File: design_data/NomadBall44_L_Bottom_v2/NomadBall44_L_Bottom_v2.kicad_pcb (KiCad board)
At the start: 2 copper layers, 149 x 96.5 mm, 57 parts, among them SW1 SW_Push, SW10 SW_Push, SW11 SW_Push, SW12 SW_Push, SW13 SW_Push, SW14 SW_Push, SW15 SW_Push, SW16 SW_Push, SW17 SW_Push, SW18 SW_Push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

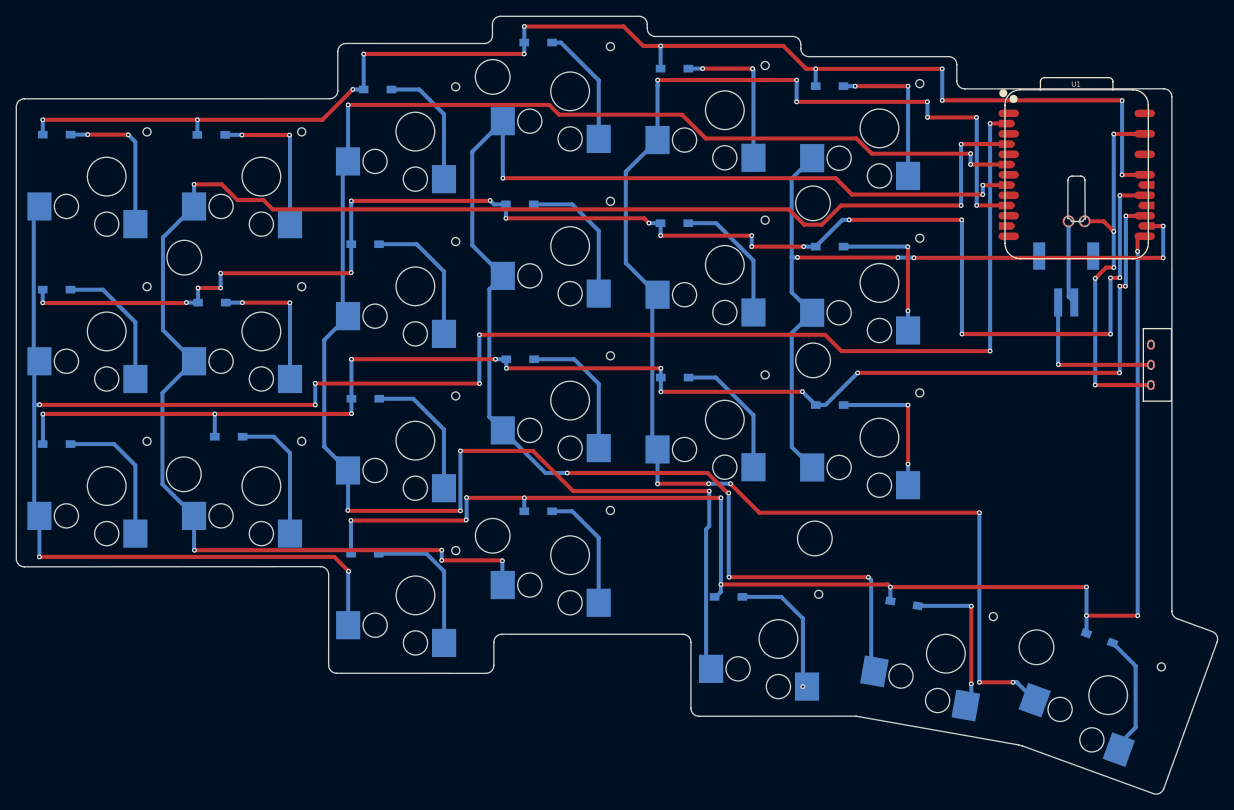
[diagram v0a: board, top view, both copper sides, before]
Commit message: 配線を削除しネジ穴を設定
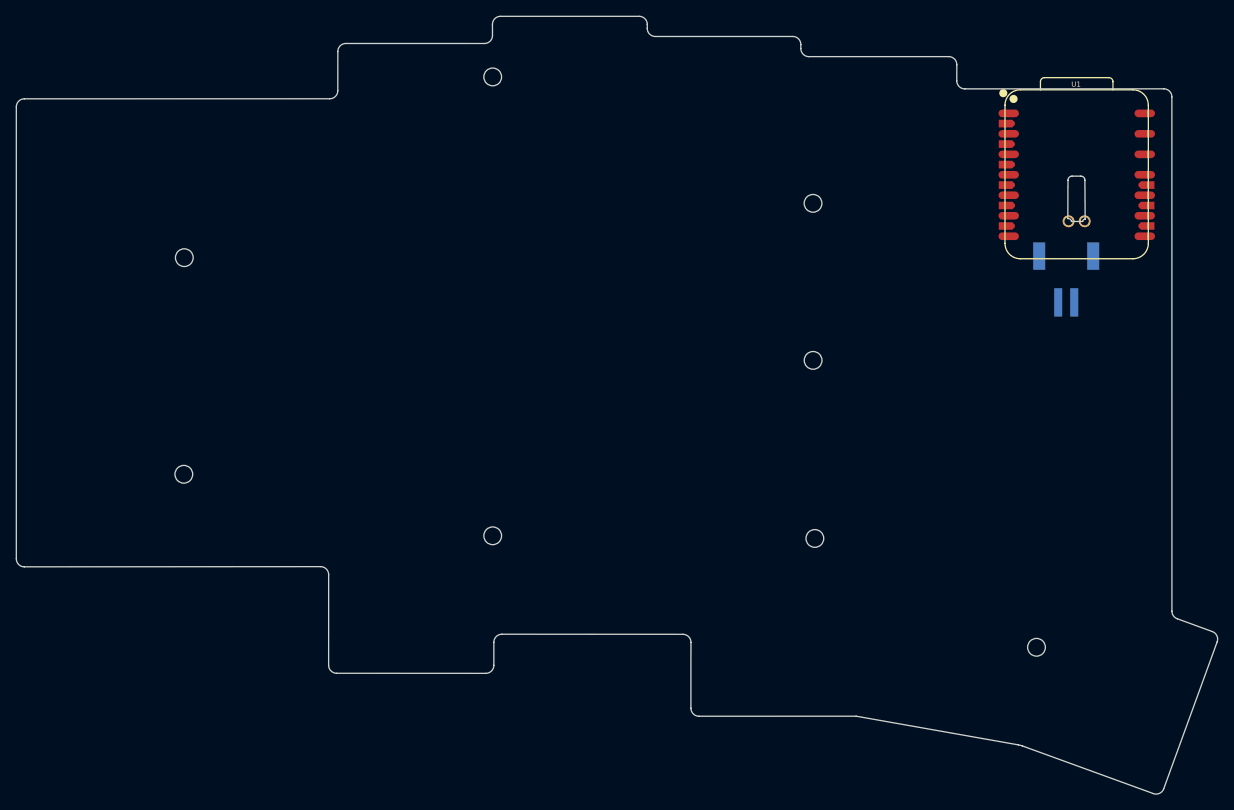
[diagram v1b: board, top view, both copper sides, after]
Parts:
- removed D1, D10, D11, D12, D13, D14, D15, D16, D17, D18, D19, D2, D20, D21, D22, D23, D3, D4, D5, D6, D7, D8, D9: D, NomadBall44:Diode_SMD
- removed SW1, SW10, SW11, SW12, SW13, SW14, SW15, SW16, SW17, SW18, SW19, SW2, SW20, SW21, SW22, SW23, SW3, SW4, SW5, SW6, SW7, SW8, SW9: SW_Push, NomadBall44:Choc_v2_Hotswap_1u
- removed SW24: SW_SPDT, NomadBall44:TGSW_MSK-12D19
- REF** (x8): value MountingHole_4.3mm_M4 -> Val**; footprint MountingHole:MountingHole_4.3mm_M4 -> NomadBall44:m2_Screw_Hole_EdgeCuts
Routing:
- net Col0: track 248.9 -> 0.01 mm, vias 9 -> 0
- net Col2: track 215.7 -> 0.03 mm, vias 7 -> 0
- net Col1: track 206.5 -> 0.00 mm, vias 7 -> 0
- net Row1: track 188.0 -> 0.03 mm, vias 21 -> 0
- net Col3: track 185.3 -> 0.03 mm, vias 7 -> 0
- net Col4: track 183.0 -> 0.01 mm, vias 13 -> 0
- net Row2: track 175.0 -> 0.03 mm, vias 14 -> 0
- net Row3: track 173.7 -> 0.13 mm, vias 11 -> 0
- net Row0: track 169.2 -> 0.01 mm, vias 12 -> 0
- net Col5: track 94.7 -> 0.03 mm, vias 5 -> 0
- net GND: track 46.7 -> 0.06 mm, vias 5 -> 0
- net Net-(D22-A): track 20.4 -> 0.00 mm, vias 2 -> 0
- net Net-(BT1--): track 19.2 -> 0.00 mm, vias 1 -> 0
- net Net-(D6-A): track 19.1 -> 0.00 mm, vias 2 -> 0
- net Net-(D2-A): track 19.1 -> 0.00 mm, vias 2 -> 0
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
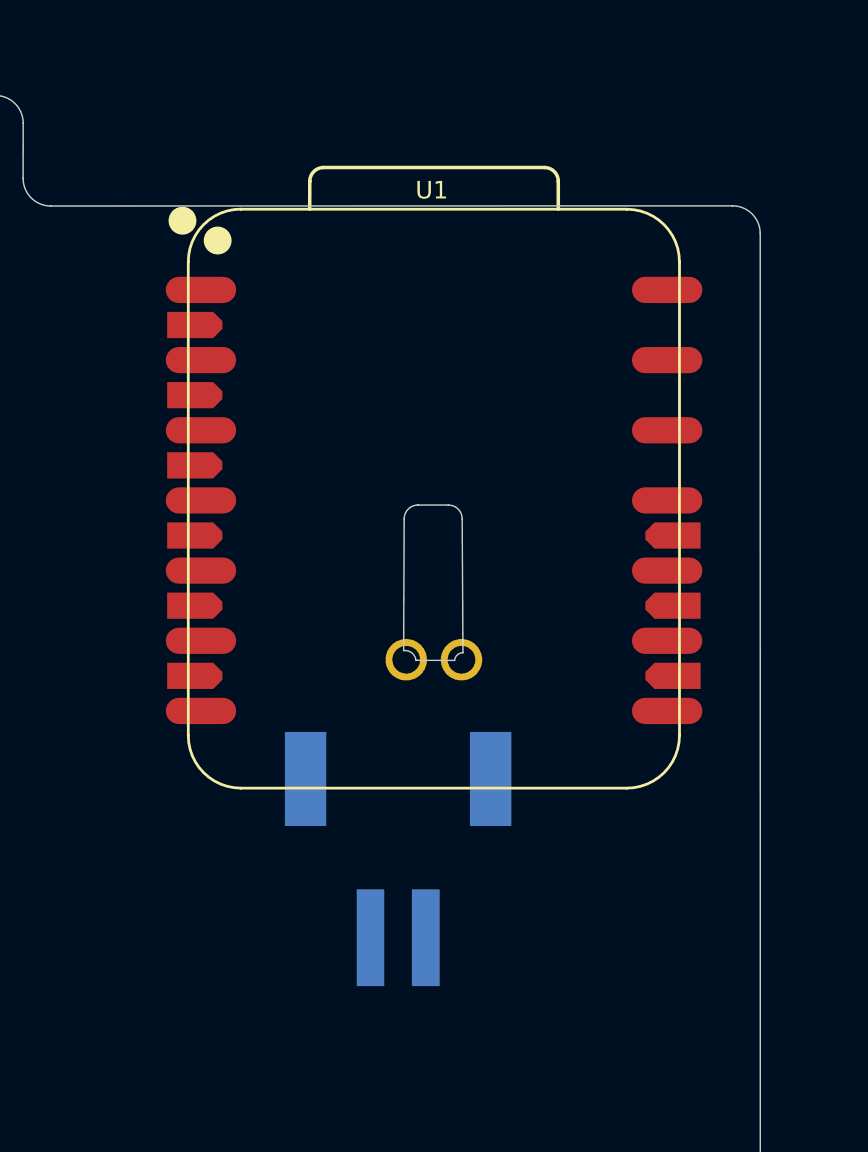
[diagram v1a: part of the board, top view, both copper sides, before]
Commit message: 不要なフットプリントを削除
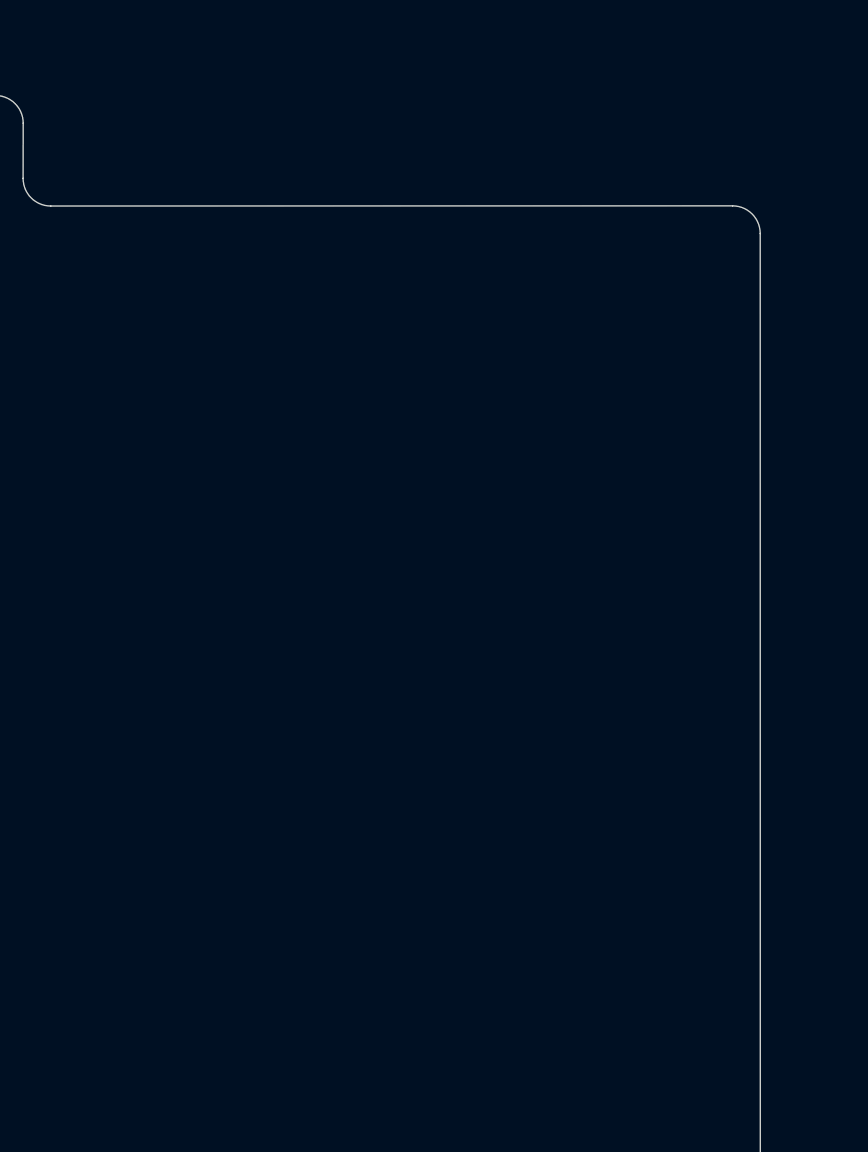
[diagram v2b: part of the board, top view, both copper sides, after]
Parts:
- removed BT1: Battery_Cell, NomadBall44:JST_S2B-PH-SM4-TB
- removed U1: XIAO-nRF52840-Plus-SMD, NomadBall44:XIAO-nRF52840-Plus-ver3
